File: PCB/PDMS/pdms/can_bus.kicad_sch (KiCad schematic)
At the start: 4 parts, among them U2 MCP2561-E-SN, U3 MCP2561-E-SN

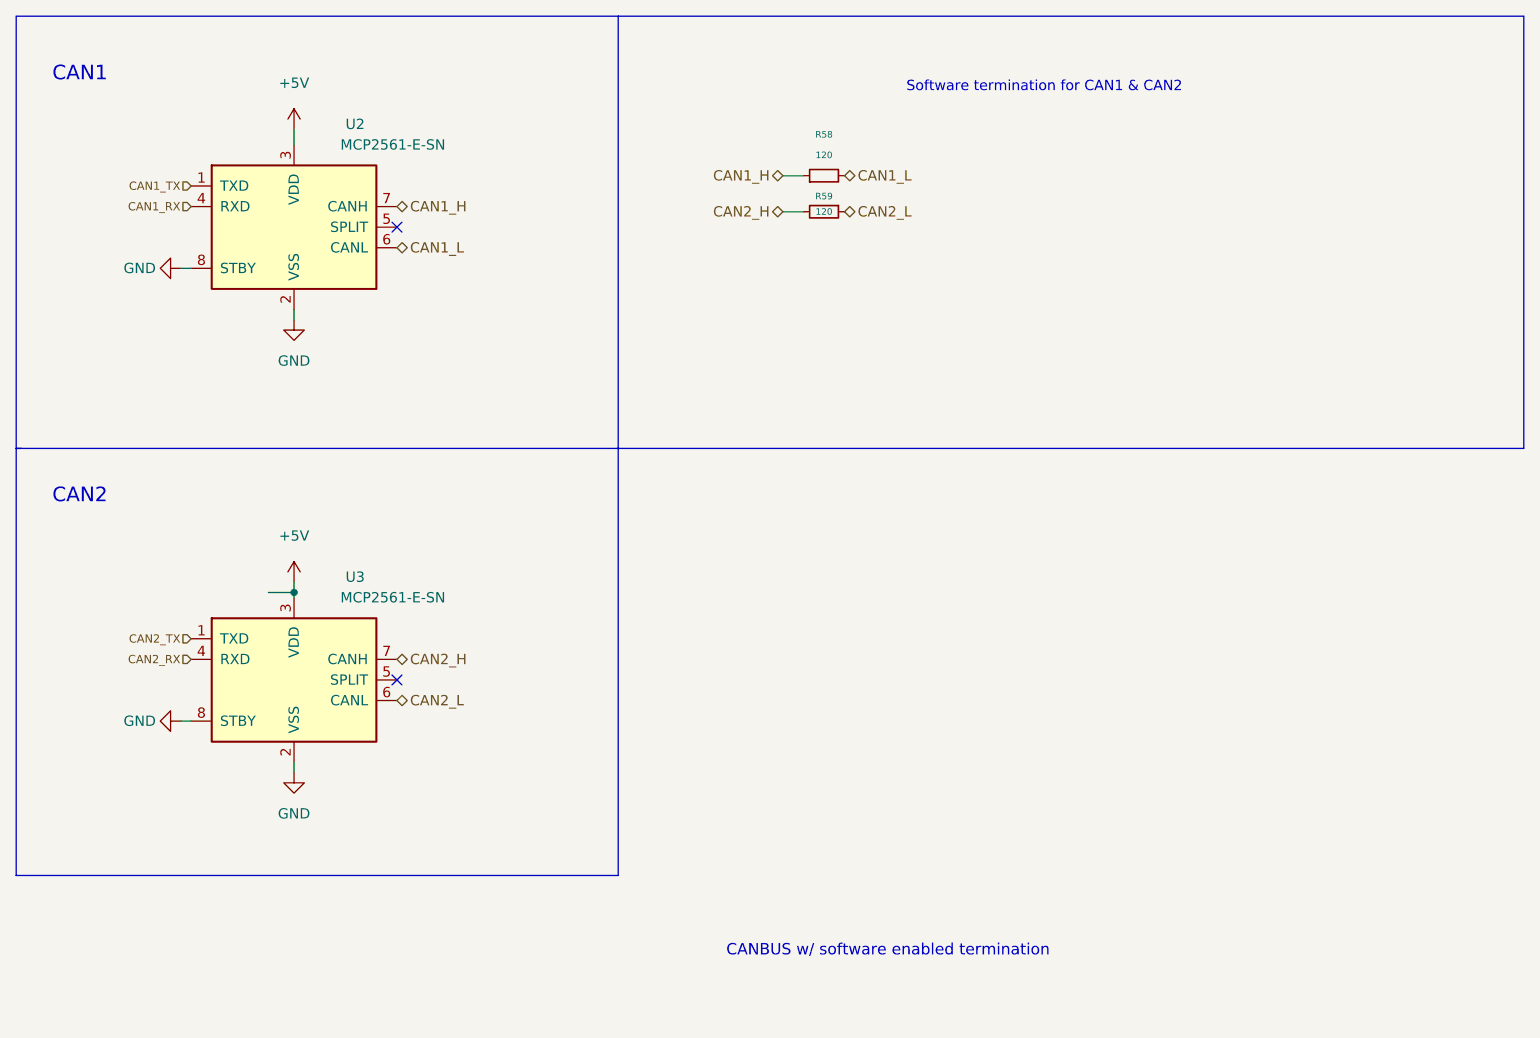
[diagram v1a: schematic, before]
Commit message: Added CAN ESD protection
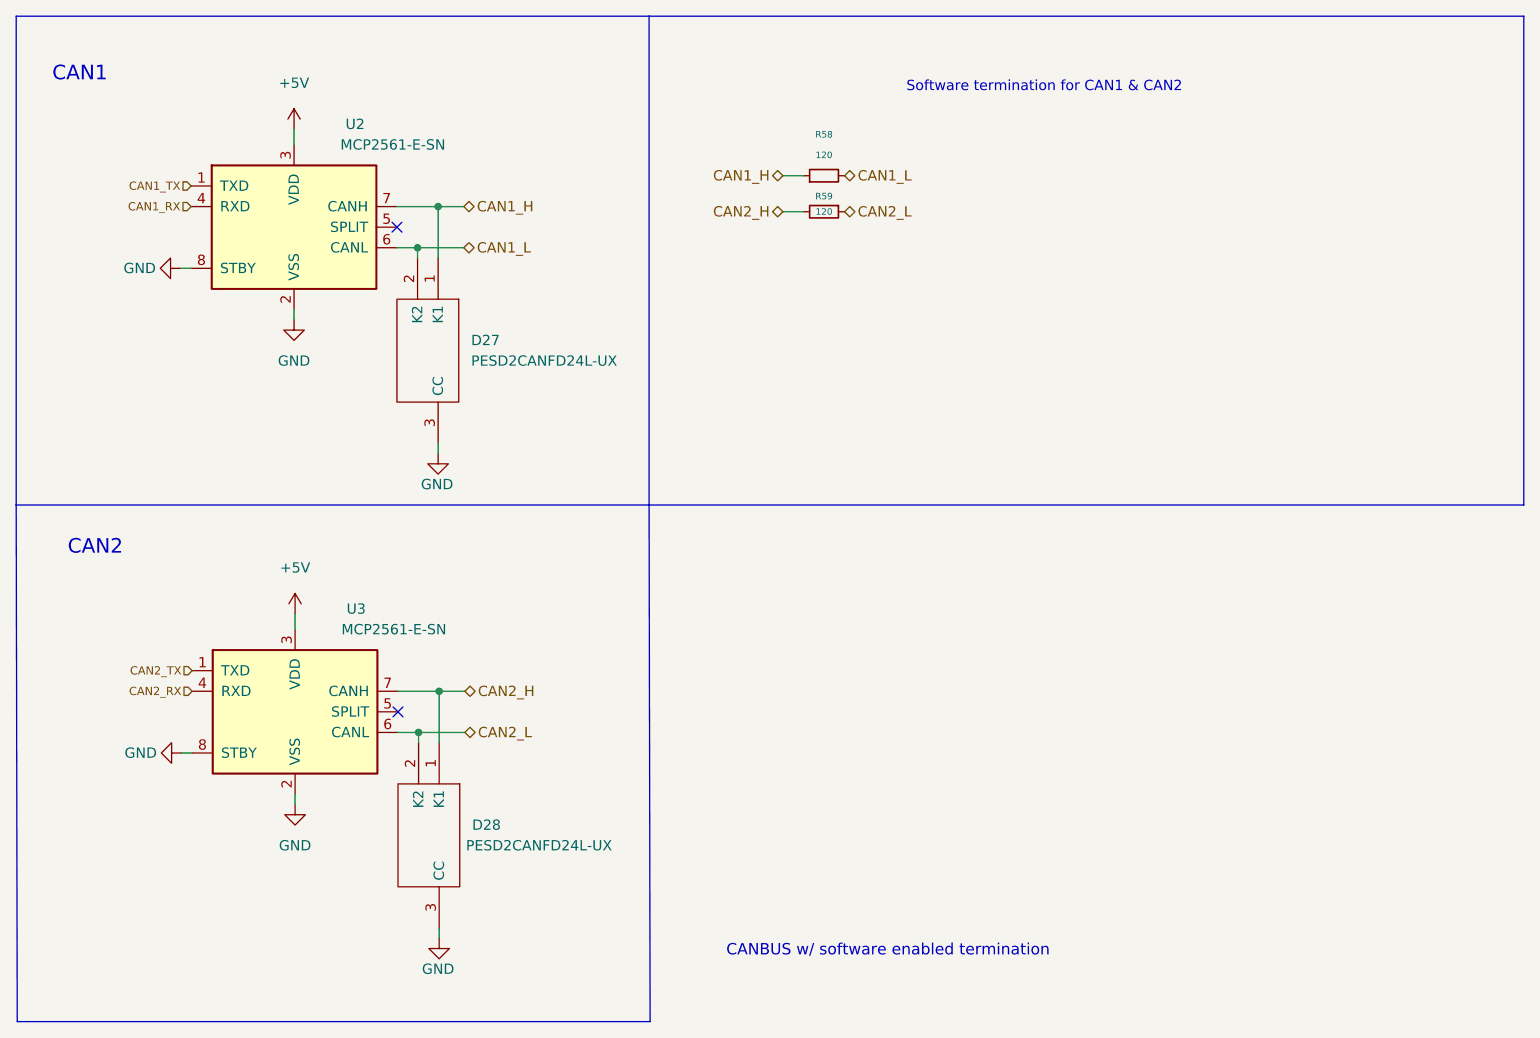
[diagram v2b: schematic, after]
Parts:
- added D27, D28: PESD2CANFD24L-UX, SOT65P210X110-3N, symbol pdms_additional:PESD2CANFD24L-UX
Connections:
- net CAN1_H: now also D27.1 (K1)
- net CAN1_L: now also D27.2 (K2)
- net CAN2_H: now also D28.1 (K1)
- net CAN2_L: now also D28.2 (K2)
- net GND: now also D27.3 (CC), D28.3 (CC)
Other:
- moved on the sheet: U3

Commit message: Added NTC section with 8-to-1 multiplexer
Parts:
- D27, D28: footprint SOT65P210X110-3N -> (none)
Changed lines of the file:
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@@
       (effects (font (size 1.27 1.27)) (justify left))
     )
-    (property "Footprint" "SOT65P210X110-3N" (id 2) (at 66.802 120.777 0)
+    (property "Footprint" "" (id 2) (at 66.802 120.777 0)
       (effects (font (size 1.27 1.27)) (justify left) hide)
     )
@@
       (effects (font (size 1.27 1.27)) (justify left))
     )
-    (property "Footprint" "SOT65P210X110-3N" (id 2) (at 66.675 60.96 0)
+    (property "Footprint" "" (id 2) (at 66.675 60.96 0)
       (effects (font (size 1.27 1.27)) (justify left) hide)
     )

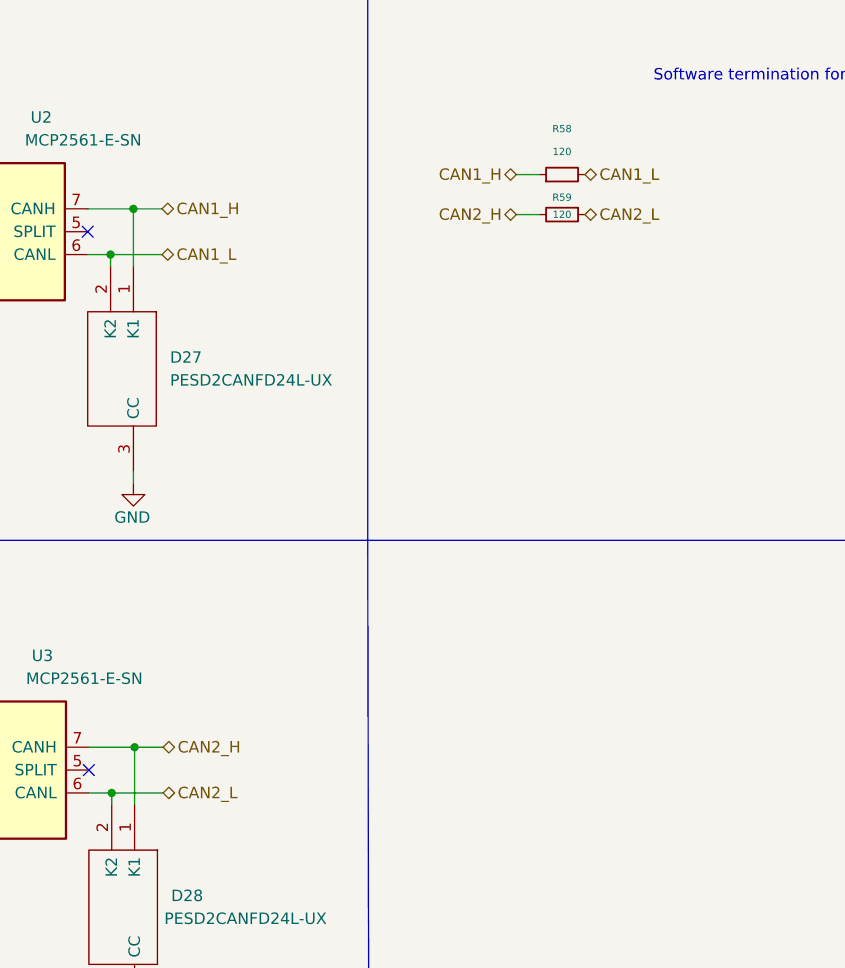
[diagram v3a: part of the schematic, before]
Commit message: Wired all peripherals
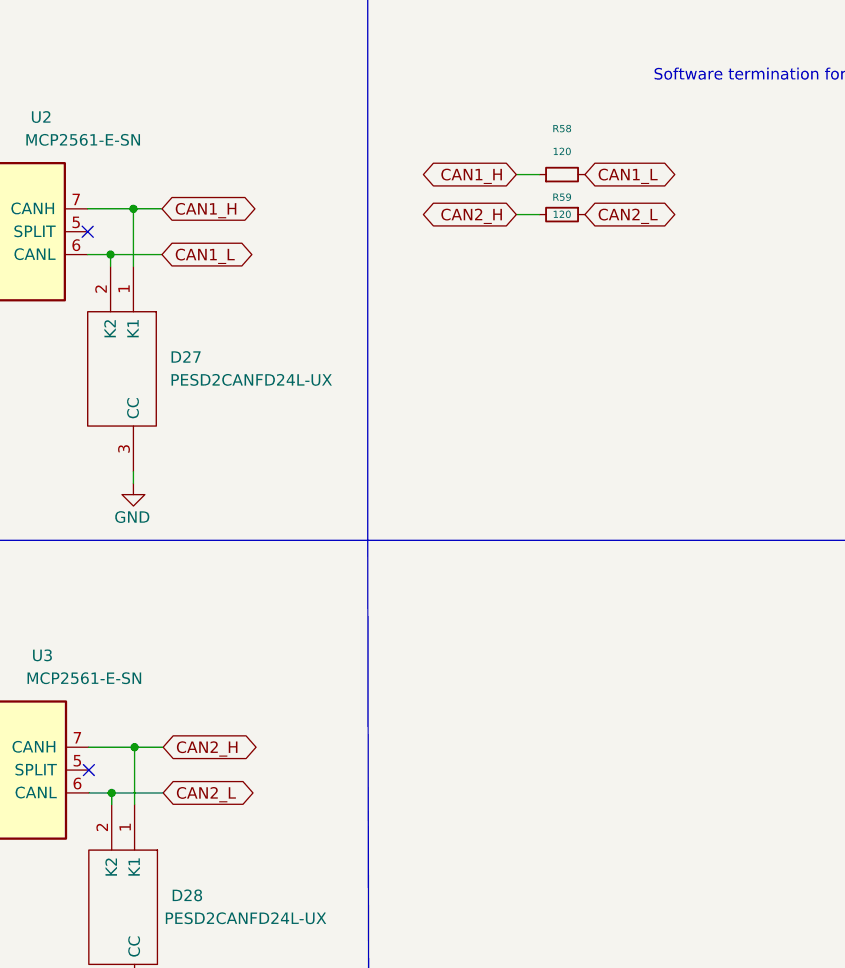
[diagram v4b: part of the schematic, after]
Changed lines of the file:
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@@
     (effects (font (size 1.8 1.8)) (justify left bottom))
   )
-  (hierarchical_label "CAN2_H" (shape bidirectional) (at 67.437 95.377 0)
+  (global_label "CAN2_L" (shape bidirectional) (at 114.3 36.195 0) (fields_autoplaced)
     (effects (font (size 1.27 1.27)) (justify left))
+    (property "Intersheet References" "${INTERSHEET_REFS}" (id 0) (at 123.6074 36.1156 0)
+      (effects (font (size 1.27 1.27)) (justify left) hide)
+    )
+  )
+  (global_label "CAN2_H" (shape bidirectional) (at 106.68 36.195 180) (fields_autoplaced)
+    (effects (font (size 1.27 1.27)) (justify right))
+    (property "Intersheet References" "${INTERSHEET_REFS}" (id 0) (at 97.0702 36.1156 0)
+      (effects (font (size 1.27 1.27)) (justify right) hide)
+    )
+  )
+  (global_label "CAN1_L" (shape bidirectional) (at 114.3 31.75 0) (fields_autoplaced)
+    (effects (font (size 1.27 1.27)) (justify left))
+    (property "Intersheet References" "${INTERSHEET_REFS}" (id 0) (at 123.6074 31.6706 0)
+      (effects (font (size 1.27 1.27)) (justify left) hide)
+    )
+  )
+  (global_label "CAN1_H" (shape bidirectional) (at 106.68 31.75 180) (fields_autoplaced)
+    (effects (font (size 1.27 1.27)) (justify right))
+    (property "Intersheet References" "${INTERSHEET_REFS}" (id 0) (at 97.0702 31.6706 0)
+      (effects (font (size 1.27 1.27)) (justify right) hide)
+    )
+  )
+  (global_label "CAN2_H" (shape bidirectional) (at 67.437 95.377 0) (fields_autoplaced)
+    (effects (font (size 1.27 1.27)) (justify left))
+    (property "Intersheet References" "${INTERSHEET_REFS}" (id 0) (at 77.0468 95.2976 0)
+      (effects (font (size 1.27 1.27)) (justify left) hide)
+    )
+  )
+  (global_label "CAN1_L" (shape bidirectional) (at 67.31 40.64 0) (fields_autoplaced)
+    (effects (font (size 1.27 1.27)) (justify left))
+    (property "Intersheet References" "${INTERSHEET_REFS}" (id 0) (at 76.6174 40.5606 0)
+      (effects (font (size 1.27 1.27)) (justify left) hide)
+    )
+  )
+  (global_label "CAN1_H" (shape bidirectional) (at 67.31 35.56 0) (fields_autoplaced)
+    (effects (font (size 1.27 1.27)) (justify left))
+    (property "Intersheet References" "${INTERSHEET_REFS}" (id 0) (at 76.9198 35.4806 0)
+      (effects (font (size 1.27 1.27)) (justify left) hide)
+    )
+  )
+  (global_label "CAN2_L" (shape bidirectional) (at 67.437 100.457 0) (fields_autoplaced)
+    (effects (font (size 1.27 1.27)) (justify left))
+    (property "Intersheet References" "${INTERSHEET_REFS}" (id 0) (at 76.7444 100.3776 0)
+      (effects (font (size 1.27 1.27)) (justify left) hide)
+    )
   )
   (hierarchical_label "CAN2_TX" (shape input) (at 33.782 92.837 180)
     (effects (font (size 1.016 1.016)) (justify right))
   )
-  (hierarchical_label "CAN1_H" (shape bidirectional) (at 67.31 35.56 0)
-    (effects (font (size 1.27 1.27)) (justify left))
-  )
-  (hierarchical_label "CAN2_H" (shape bidirectional) (at 106.68 36.195 180)
-    (effects (font (size 1.27 1.27)) (justify right))
-  )
   (hierarchical_label "CAN1_TX" (shape input) (at 33.655 33.02 180)
     (effects (font (size 1.016 1.016)) (justify right))
-  )
-  (hierarchical_label "CAN1_L" (shape bidirectional) (at 114.3 31.75 0)
-    (effects (font (size 1.27 1.27)) (justify left))
-  )
-  (hierarchical_label "CAN1_L" (shape bidirectional) (at 67.31 40.64 0)
-    (effects (font (size 1.27 1.27)) (justify left))
   )
   (hierarchical_label "CAN1_RX" (shape input) (at 33.655 35.56 180)
     (effects (font (size 1.016 1.016)) (justify right))
   )
-  (hierarchical_label "CAN2_L" (shape bidirectional) (at 67.437 100.457 0)
-    (effects (font (size 1.27 1.27)) (justify left))
-  )
   (hierarchical_label "CAN2_RX" (shape input) (at 33.782 95.377 180)
     (effects (font (size 1.016 1.016)) (justify right))
   )
-  (hierarchical_label "CAN1_H" (shape bidirectional) (at 106.68 31.75 180)
-    (effects (font (size 1.27 1.27)) (justify right))
-  )
-  (hierarchical_label "CAN2_L" (shape bidirectional) (at 114.3 36.195 0)
-    (effects (font (size 1.27 1.27)) (justify left))
-  )
   (symbol (lib_id "power:GND") (at 64.262 125.857 0) (mirror y) (unit 1)

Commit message: Mostly assigned footprints
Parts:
- D27, D28: footprint (none) -> PDMS_Additional:SOT65P210X110-3N
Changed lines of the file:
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@@
       (effects (font (size 1.27 1.27)) (justify left))
     )
-    (property "Footprint" "" (id 2) (at 66.802 120.777 0)
+    (property "Footprint" "PDMS_Additional:SOT65P210X110-3N" (id 2) (at 66.802 120.777 0)
       (effects (font (size 1.27 1.27)) (justify left) hide)
     )
@@
       (effects (font (size 1.27 1.27)) (justify left))
     )
-    (property "Footprint" "" (id 2) (at 66.675 60.96 0)
+    (property "Footprint" "PDMS_Additional:SOT65P210X110-3N" (id 2) (at 66.675 60.96 0)
       (effects (font (size 1.27 1.27)) (justify left) hide)
     )

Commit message: Added connector and more
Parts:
- R58, R59: footprint Resistor_SMD:R_0402_1005Metric_Pad0.72x0.64mm_HandSolder -> Resistor_SMD:R_0402_1005Metric
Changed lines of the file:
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@@
       (effects (font (size 0.8 0.8)))
     )
-    (property "Footprint" "Resistor_SMD:R_0402_1005Metric_Pad0.72x0.64mm_HandSolder" (id 2) (at 111.76 36.195 0)
+    (property "Footprint" "Resistor_SMD:R_0402_1005Metric" (id 2) (at 111.76 36.195 0)
       (effects (font (size 1.27 1.27)) hide)
     )
@@
       (effects (font (size 0.8 0.8)))
     )
-    (property "Footprint" "Resistor_SMD:R_0402_1005Metric_Pad0.72x0.64mm_HandSolder" (id 2) (at 111.76 31.75 0)
+    (property "Footprint" "Resistor_SMD:R_0402_1005Metric" (id 2) (at 111.76 31.75 0)
       (effects (font (size 1.27 1.27)) hide)
     )

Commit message: Steady layout
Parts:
- added C64, C65: 100nF, Capacitor_SMD:C_0402_1005Metric_Pad0.74x0.62mm_HandSolder, symbol Device:C_Small
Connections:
- net +5V: now also C64.1, C65.1
- net GND: now also C64.2, C65.2
